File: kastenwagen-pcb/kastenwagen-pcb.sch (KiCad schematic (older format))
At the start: 9 parts

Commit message: Complete Schema
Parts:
- added D100, D101, D120, D121, D140, D141, D160, D170, D181, D202, D203, D222, D223, D242, D243, D262, D272, D273, D304, D305, D324, D325, D344, D345, D364, D374, D375, D406, D407, D437, D446, D457, D476, D477: BAV70, Keebio-Parts:SOT-23_Handsoldering, symbol Diode:BAV70
- added MX101, MX110, MX111, MX120, MX121, MX130, MX131, MX140, MX141, MX150, MX151, MX170, MX171, MX180, MX181, MX203, MX212, MX213, MX222, MX223, MX232, MX233, MX242, MX243, MX252, MX253, MX272, MX273, MX282, MX283, MX305, MX314, MX315, MX324, MX325, MX334, MX335, MX344, MX345, MX354, MX364, MX374, MX375, MX384, MX385, MX416, MX446, MX457, MX467, MX476, MX477, MX486, MX487: MX-NoLED, MX_Only:MXOnly-1U-NoLED, symbol MX_Alps_Hybrid:MX-NoLED
- added MX160, MX304: MX-NoLED, MX_Only:MXOnly-1.75U-NoLED, symbol MX_Alps_Hybrid:MX-NoLED
- added MX202, MX355, MX406, MX407, MX447, MX456: MX-NoLED, MX_Only:MXOnly-1.25U-NoLED, symbol MX_Alps_Hybrid:MX-NoLED
- added MX262: MX-NoLED, MX_Only:MXOnly-1.5U-NoLED, symbol MX_Alps_Hybrid:MX-NoLED
- added MX283.200, MX487.200: MX-NoLED, MX_Only:MXOnly-2U-ReversedStabilizers-NoLED, symbol MX_Alps_Hybrid:MX-NoLED
- added MX417: MX-NoLED, MX_Only:MXOnly-2.75U-NoLED, symbol MX_Alps_Hybrid:MX-NoLED
- added MX417.700: MX-NoLED, MX_Only:MXOnly-7U-NoLED, symbol MX_Alps_Hybrid:MX-NoLED
- added MX437: MX-NoLED, MX_Only:MXOnly-2.25U-NoLED, symbol MX_Alps_Hybrid:MX-NoLED
- added MX477.200: MX-NoLED, MX_Only:MXOnly-2U-NoLED, symbol MX_Alps_Hybrid:MX-NoLED
- added RSW100, RSW181: Rotary_Encoder_Switch, Keebio-Parts:RotaryEncoder_Alps_EC11E-Switch_Vertical_H20mm, symbol Device:Rotary_Encoder_Switch
- D1, D2, D3: footprint (none) -> LED_THT:LED_D3.0mm
- MX100: footprint (none) -> MX_Only:MXOnly-1U-NoLED
- R1, R2, R3: footprint (none) -> Keebio-Parts:Resistor-Hybrid-Back
- SW1: renamed from SW?; footprint (none) -> Keebio-Parts:SW_Tactile_SPST_Angled_MJTP1117
- U1: renamed from U?; footprint (none) -> Keebio-Parts:Elite-C-castellated-29pin-holes
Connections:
- net Col0: now also MX100.1 (COL), U1.20 (A3/PF4), MX101.1 (COL), MX202.1 (COL), MX203.1 (COL), MX304.1 (COL), MX305.1 (COL), MX406.1 (COL), MX407.1 (COL), RSW100.S2
- net Col1: now also U1.19 (A2/PF5), MX110.1 (COL), MX111.1 (COL), MX212.1 (COL), MX213.1 (COL), MX314.1 (COL), MX315.1 (COL), MX416.1 (COL), MX417.1 (COL), MX417.700.1 (COL)
- net Col2: now also U1.18 (A1/PF6), MX120.1 (COL), MX121.1 (COL), MX222.1 (COL), MX223.1 (COL), MX324.1 (COL), MX325.1 (COL)
- net Col3: now also U1.17 (A0/PF7), MX130.1 (COL), MX131.1 (COL), MX232.1 (COL), MX233.1 (COL), MX334.1 (COL), MX335.1 (COL), MX437.1 (COL)
- net Col4: now also U1.16 (15/PB1), MX140.1 (COL), MX141.1 (COL), MX242.1 (COL), MX243.1 (COL), MX344.1 (COL), MX345.1 (COL), MX446.1 (COL), MX447.1 (COL)
- net Col5: now also U1.15 (14/PB3), MX150.1 (COL), MX151.1 (COL), MX252.1 (COL), MX253.1 (COL), MX354.1 (COL), MX355.1 (COL), MX456.1 (COL), MX457.1 (COL)
- net Col6: now also U1.14 (16/PB2), MX160.1 (COL), MX262.1 (COL), MX364.1 (COL), MX467.1 (COL)
- net Col7: now also U1.10 (7/PE6), MX170.1 (COL), MX171.1 (COL), MX272.1 (COL), MX273.1 (COL), MX374.1 (COL), MX375.1 (COL), MX476.1 (COL), MX477.1 (COL), MX477.200.1 (COL)
- net Col8: now also U1.9 (6/PD7), MX180.1 (COL), MX181.1 (COL), MX282.1 (COL), MX283.1 (COL), MX283.200.1 (COL), MX384.1 (COL), MX385.1 (COL), MX486.1 (COL), MX487.1 (COL), MX487.200.1 (COL), RSW181.S2
- net GND: now also RSW100.C, RSW181.C
- net LED1: now also U1.24 (B0)
- net LED2: now also U1.7 (4/PD4)
- net LED3: now also U1.8 (5/PC6)
- net Row0: now also U1.11 (8/PB4), D100.3 (K), D120.3 (K), D140.3 (K), D160.3 (K), D170.3 (K)
- net Row1: now also U1.12 (9/PB5), D101.3 (K), D121.3 (K), D141.3 (K), D181.3 (K)
- net Rotary1A: now reaches U1.1 (TX0/PD3)
- net Rotary1A: now also RSW181.A
- net Row7: now reaches U1.13 (10/PB6)
- net Row7: now also D407.3 (K), D437.3 (K), D457.3 (K), D477.3 (K)
- net Rotary1B: now reaches U1.2 (RX1/PD2)
- net Rotary1B: now also RSW181.B
- net Row2: now reaches U1.25 (B7)
- net Row2: now also D202.3 (K), D222.3 (K), D242.3 (K), D262.3 (K), D272.3 (K)
- net Row3: now reaches U1.26 (D5)
- net Row3: now also D203.3 (K), D223.3 (K), D243.3 (K), D273.3 (K)
- net Row4: now reaches U1.27 (C7)
- net Row4: now also D304.3 (K), D324.3 (K), D344.3 (K), D364.3 (K), D374.3 (K)
- net Row5: now reaches U1.28 (F1)
- net Row5: now also D305.3 (K), D325.3 (K), D345.3 (K), D375.3 (K)
- net Row6: now reaches U1.29 (F0)
- net Row6: now also D406.3 (K), D446.3 (K), D476.3 (K)
- net Rotary0A: now reaches U1.5 (2/PD1)
- net Rotary0A: now also RSW100.A
- net Rotary0B: now reaches U1.6 (3/PD0)
- net Rotary0B: now also RSW100.B
- net at MX100.2 (ROW): now also D100.1 (A), RSW100.S1
- new net: D101.1 (A), MX101.2 (ROW)
- new net: D100.2 (A), MX110.2 (ROW)
- new net: D101.2 (A), MX111.2 (ROW)
- new net: D120.1 (A), MX120.2 (ROW)
- new net: D121.1 (A), MX121.2 (ROW)
- new net: D120.2 (A), MX130.2 (ROW)
- new net: D121.2 (A), MX131.2 (ROW)
- new net: D140.1 (A), MX140.2 (ROW)
- new net: D141.1 (A), MX141.2 (ROW)
- new net: D140.2 (A), MX150.2 (ROW)
- new net: D141.2 (A), MX151.2 (ROW)
- new net: D160.1 (A), MX160.2 (ROW)
- new net: D170.1 (A), MX170.2 (ROW)
- new net: D181.1 (A), MX171.2 (ROW)
- new net: D170.2 (A), MX180.2 (ROW)
- new net: D181.2 (A), MX181.2 (ROW), RSW181.S1
- new net: D202.1 (A), MX202.2 (ROW)
- new net: D203.1 (A), MX203.2 (ROW)
- new net: D202.2 (A), MX212.2 (ROW)
- new net: D203.2 (A), MX213.2 (ROW)
- new net: D222.1 (A), MX222.2 (ROW)
- new net: D223.1 (A), MX223.2 (ROW)
- new net: D222.2 (A), MX232.2 (ROW)
- new net: D223.2 (A), MX233.2 (ROW)
- new net: D242.1 (A), MX242.2 (ROW)
- new net: D243.1 (A), MX243.2 (ROW)
- new net: D242.2 (A), MX252.2 (ROW)
- new net: D243.2 (A), MX253.2 (ROW)
- new net: D262.1 (A), MX262.2 (ROW)
- new net: D272.1 (A), MX272.2 (ROW)
- new net: D273.1 (A), MX273.2 (ROW)
- new net: D272.2 (A), MX282.2 (ROW)
- new net: D273.2 (A), MX283.2 (ROW), MX283.200.2 (ROW)
- new net: D304.1 (A), MX304.2 (ROW)
- new net: D305.1 (A), MX305.2 (ROW)
- new net: D304.2 (A), MX314.2 (ROW)
- new net: D305.2 (A), MX315.2 (ROW)
- new net: D324.1 (A), MX324.2 (ROW)
- new net: D325.1 (A), MX325.2 (ROW)
- new net: D324.2 (A), MX334.2 (ROW)
- new net: D325.2 (A), MX335.2 (ROW)
- new net: D344.1 (A), MX344.2 (ROW)
- new net: D345.1 (A), MX345.2 (ROW)
- new net: D344.2 (A), MX354.2 (ROW)
- new net: D345.2 (A), MX355.2 (ROW)
- new net: D364.1 (A), MX364.2 (ROW)
- new net: D374.1 (A), MX374.2 (ROW)
- new net: D375.1 (A), MX375.2 (ROW)
- new net: D374.2 (A), MX384.2 (ROW)
- new net: D375.2 (A), MX385.2 (ROW)
- new net: D406.1 (A), MX406.2 (ROW)
- new net: D407.1 (A), MX407.2 (ROW)
- new net: D406.2 (A), MX416.2 (ROW)
- new net: D407.2 (A), MX417.2 (ROW), MX417.700.2 (ROW)
- new net: D437.1 (A), MX437.2 (ROW)
- new net: D437.2 (A), MX447.2 (ROW)
- new net: D446.1 (A), MX446.2 (ROW)
- new net: D446.2 (A), MX456.2 (ROW)
- new net: D457.1 (A), MX457.2 (ROW)
- new net: D457.2 (A), MX467.2 (ROW)
- new net: D476.1 (A), MX476.2 (ROW)
- new net: D477.1 (A), MX477.2 (ROW), MX477.200.2 (ROW)
- new net: D476.2 (A), MX486.2 (ROW)
- new net: D477.2 (A), MX487.2 (ROW), MX487.200.2 (ROW)
- no-connect marks 1 -> 4
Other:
- moved on the sheet: D1, D2, D3, MX100, SW1, U1

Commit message: first draft routing
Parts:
- removed MX283.200: MX-NoLED, MX_Only:MXOnly-2U-ReversedStabilizers-NoLED, symbol MX_Alps_Hybrid:MX-NoLED
- RSW100, RSW181: footprint Keebio-Parts:RotaryEncoder_Alps_EC11E-Switch_Vertical_H20mm -> Keebio-Parts:RotaryEncoder_EC11-no-legs
- renumbered D181 to D171
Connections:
- net Rotary0A: now also U1.6 (3/PD0); no longer U1.5 (2/PD1)
- net Rotary0B: now also U1.5 (2/PD1); no longer U1.6 (3/PD0)
- net at MX160.2 (ROW): now also D160.2 (A); no longer D160.1 (A)
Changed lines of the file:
@@
 	1    0    0    -1
 $EndComp
-Wire Wire Line
-	8300 1500 8300 1800
-NoConn ~ 8900 1800
+NoConn ~ 8300 1800
 $Comp
 L MX_Alps_Hybrid:MX-NoLED MX170
@@
 $EndComp
 $Comp
-L Diode:BAV70 D181
+L Diode:BAV70 D171
 U 1 1 6043B80A
 P 10800 1900
-F 0 "D181" H 10800 2117 50  0000 C CNN
+F 0 "D171" H 10800 2117 50  0000 C CNN
 F 1 "BAV70" H 10800 2026 50  0000 C CNN
 F 2 "Keebio-Parts:SOT-23_Handsoldering" H 10800 1900 50  0001 C CNN
@@
 	11150 1300 11150 2500
 Connection ~ 11150 1300
-$Comp
-L MX_Alps_Hybrid:MX-NoLED MX283.200
-U 1 1 6049446A
-P 11950 2850
-F 0 "MX283.200" H 11983 3073 60  0000 C CNN
-F 1 "MX-NoLED" H 11983 2999 20  0000 C CNN
-F 2 "MX_Only:MXOnly-2U-ReversedStabilizers-NoLED" H 11325 2825 60  0001 C CNN
-F 3 "" H 11325 2825 60  0001 C CNN
-	1    11950 2850
-	1    0    0    -1
-$EndComp
-Wire Wire Line
-	12100 2800 12300 2800
-Wire Wire Line
-	12300 2800 12300 2500
-Wire Wire Line
-	12300 2500 11600 2500
-Connection ~ 11600 2500
-Wire Wire Line
-	11900 3000 11900 3400
-Wire Wire Line
-	11900 3400 11400 3400
-Connection ~ 11400 3400
 Text GLabel 1750 3500 0    50   Input ~ 0
 Row2
@@
 F 0 "RSW181" H 12350 1183 50  0000 C CNN
 F 1 "Rotary_Encoder_Switch" H 12350 1274 50  0000 C CNN
-F 2 "Keebio-Parts:RotaryEncoder_Alps_EC11E-Switch_Vertical_H20mm" H 12200 1710 50  0001 C CNN
+F 2 "Keebio-Parts:RotaryEncoder_EC11-no-legs" H 12200 1710 50  0001 C CNN
 F 3 "~" H 12350 1810 50  0001 C CNN
 	1    12350 1550
@@
 Text GLabel 1750 8800 0    50   Input ~ 0
 Rotary1B
+Text GLabel 1750 9200 0    50   Input ~ 0
+Rotary0A
 Text GLabel 1750 9100 0    50   Input ~ 0
-Rotary0A
-Text GLabel 1750 9200 0    50   Input ~ 0
 Rotary0B
 Text GLabel 12650 1650 2    50   Input ~ 0
@@
 F 0 "RSW100" H 1000 1133 50  0000 C CNN
 F 1 "Rotary_Encoder_Switch" H 1000 1224 50  0000 C CNN
-F 2 "Keebio-Parts:RotaryEncoder_Alps_EC11E-Switch_Vertical_H20mm" H 850 1660 50  0001 C CNN
+F 2 "Keebio-Parts:RotaryEncoder_EC11-no-legs" H 850 1660 50  0001 C CNN
 F 3 "~" H 1000 1760 50  0001 C CNN
 	1    1000 1500
@@
 Wire Wire Line
 	5200 10750 5350 10750
+Wire Wire Line
+	8300 1500 8900 1500
+Wire Wire Line
+	8900 1500 8900 1800
 $EndSCHEMATC

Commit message: Reverse the stabilizers
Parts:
- MX417: footprint MX_Only:MXOnly-2.75U-NoLED -> MX_Only:MXOnly-2.75U-ReversedStabilizers-NoLED
- MX417.700: footprint MX_Only:MXOnly-7U-NoLED -> MX_Only:MXOnly-7U-ReversedStabilizers-NoLED
- MX437: footprint MX_Only:MXOnly-2.25U-NoLED -> MX_Only:MXOnly-2.25U-ReversedStabilizers-NoLED
- MX477.200: footprint MX_Only:MXOnly-2U-NoLED -> MX_Only:MXOnly-2U-ReversedStabilizers-NoLED
- MX487.200: footprint MX_Only:MXOnly-2U-ReversedStabilizers-NoLED -> MX_Only:MXOnly-2U-NoLED
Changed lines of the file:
@@
 F 0 "MX417" H 3650 6100 60  0000 C CNN
 F 1 "MX-NoLED" H 3683 5999 20  0000 C CNN
-F 2 "MX_Only:MXOnly-2.75U-NoLED" H 3025 5825 60  0001 C CNN
+F 2 "MX_Only:MXOnly-2.75U-ReversedStabilizers-NoLED" H 3025 5825 60  0001 C CNN
 F 3 "" H 3025 5825 60  0001 C CNN
 	1    3650 5850
@@
 F 0 "MX487.200" H 11983 6073 60  0000 C CNN
 F 1 "MX-NoLED" H 11983 5999 20  0000 C CNN
-F 2 "MX_Only:MXOnly-2U-ReversedStabilizers-NoLED" H 11325 5825 60  0001 C CNN
+F 2 "MX_Only:MXOnly-2U-NoLED" H 11325 5825 60  0001 C CNN
 F 3 "" H 11325 5825 60  0001 C CNN
 	1    11950 5850
@@
 F 0 "MX417.700" H 4100 6100 60  0000 C CNN
 F 1 "MX-NoLED" H 4133 5999 20  0000 C CNN
-F 2 "MX_Only:MXOnly-7U-NoLED" H 3475 5825 60  0001 C CNN
+F 2 "MX_Only:MXOnly-7U-ReversedStabilizers-NoLED" H 3475 5825 60  0001 C CNN
 F 3 "" H 3475 5825 60  0001 C CNN
 	1    4100 5850
@@
 F 0 "MX437" H 5250 6100 60  0000 C CNN
 F 1 "MX-NoLED" H 5283 5999 20  0000 C CNN
-F 2 "MX_Only:MXOnly-2.25U-NoLED" H 4625 5825 60  0001 C CNN
+F 2 "MX_Only:MXOnly-2.25U-ReversedStabilizers-NoLED" H 4625 5825 60  0001 C CNN
 F 3 "" H 4625 5825 60  0001 C CNN
 	1    5250 5850
@@
 F 0 "MX477.200" H 10000 6100 60  0000 C CNN
 F 1 "MX-NoLED" H 10033 5999 20  0000 C CNN
-F 2 "MX_Only:MXOnly-2U-NoLED" H 9375 5825 60  0001 C CNN
+F 2 "MX_Only:MXOnly-2U-ReversedStabilizers-NoLED" H 9375 5825 60  0001 C CNN
 F 3 "" H 9375 5825 60  0001 C CNN
 	1    10000 5850

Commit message: drawing edge cuts
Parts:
- D1, D2, D3: footprint LED_THT:LED_D3.0mm -> LED_SMD:LED_1206_3216Metric_Pad1.42x1.75mm_HandSolder
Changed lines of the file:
@@
 F 0 "D1" H 5043 9795 50  0000 C CNN
 F 1 "LED" H 5043 9886 50  0000 C CNN
-F 2 "LED_THT:LED_D3.0mm" H 5050 10050 50  0001 C CNN
+F 2 "LED_SMD:LED_1206_3216Metric_Pad1.42x1.75mm_HandSolder" H 5050 10050 50  0001 C CNN
 F 3 "~" H 5050 10050 50  0001 C CNN
 	1    5050 10050
@@
 F 0 "D2" H 5043 10145 50  0000 C CNN
 F 1 "LED" H 5043 10236 50  0000 C CNN
-F 2 "LED_THT:LED_D3.0mm" H 5050 10400 50  0001 C CNN
+F 2 "LED_SMD:LED_1206_3216Metric_Pad1.42x1.75mm_HandSolder" H 5050 10400 50  0001 C CNN
 F 3 "~" H 5050 10400 50  0001 C CNN
 	1    5050 10400
@@
 F 0 "D3" H 5043 10495 50  0000 C CNN
 F 1 "LED" H 5043 10586 50  0000 C CNN
-F 2 "LED_THT:LED_D3.0mm" H 5050 10750 50  0001 C CNN
+F 2 "LED_SMD:LED_1206_3216Metric_Pad1.42x1.75mm_HandSolder" H 5050 10750 50  0001 C CNN
 F 3 "~" H 5050 10750 50  0001 C CNN
 	1    5050 10750

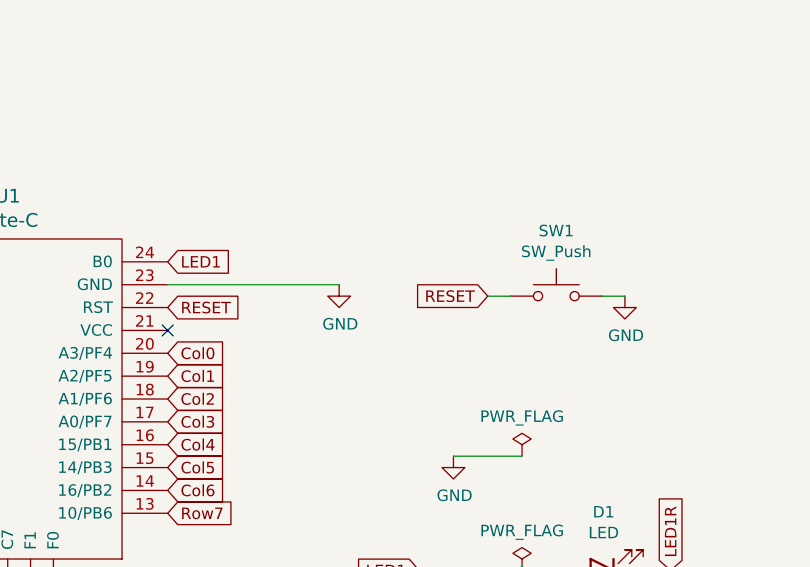
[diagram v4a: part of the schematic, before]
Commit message: Ground planes
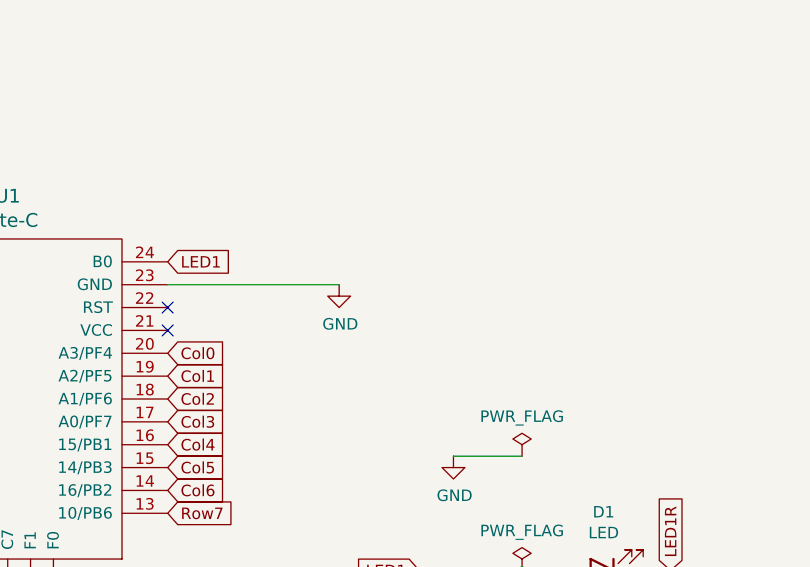
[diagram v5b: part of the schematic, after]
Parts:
- removed SW1: SW_Push, Keebio-Parts:SW_Tactile_SPST_Angled_MJTP1117, symbol Switch:SW_Push
- R1, R2, R3: footprint Keebio-Parts:Resistor-Hybrid-Back -> Keebio-Parts:R_0805
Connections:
- net RESET: no longer names the net of U1.22 (RST)
- no-connect marks 4 -> 5
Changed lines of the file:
@@
 Wire Wire Line
 	3900 8800 3150 8800
-$Comp
-L Switch:SW_Push SW1
-U 1 1 60414731
-P 4850 8850
-F 0 "SW1" H 4850 9135 50  0000 C CNN
-F 1 "SW_Push" H 4850 9044 50  0000 C CNN
-F 2 "Keebio-Parts:SW_Tactile_SPST_Angled_MJTP1117" H 4850 9050 50  0001 C CNN
-F 3 "~" H 4850 9050 50  0001 C CNN
-	1    4850 8850
-	1    0    0    -1
-$EndComp
-Text GLabel 3150 8900 2    50   Input ~ 0
-RESET
-Text GLabel 4550 8850 0    50   Input ~ 0
-RESET
-Wire Wire Line
-	4550 8850 4650 8850
-$Comp
-L power:GND #PWR0104
-U 1 1 60414DCC
-P 5150 8850
-F 0 "#PWR0104" H 5150 8600 50  0001 C CNN
-F 1 "GND" H 5155 8677 50  0000 C CNN
-F 2 "" H 5150 8850 50  0001 C CNN
-F 3 "" H 5150 8850 50  0001 C CNN
-	1    5150 8850
-	1    0    0    -1
-$EndComp
-Wire Wire Line
-	5150 8850 5050 8850
 NoConn ~ 3150 9000
 $Comp
@@
 F 0 "R1" V 6493 10050 50  0000 C CNN
 F 1 "470" V 6584 10050 50  0000 C CNN
-F 2 "Keebio-Parts:Resistor-Hybrid-Back" V 6630 10050 50  0001 C CNN
+F 2 "Keebio-Parts:R_0805" V 6630 10050 50  0001 C CNN
 F 3 "~" H 6700 10050 50  0001 C CNN
 	1    6700 10050
@@
 F 0 "R2" V 6493 10400 50  0000 C CNN
 F 1 "470" V 6584 10400 50  0000 C CNN
-F 2 "Keebio-Parts:Resistor-Hybrid-Back" V 6630 10400 50  0001 C CNN
+F 2 "Keebio-Parts:R_0805" V 6630 10400 50  0001 C CNN
 F 3 "~" H 6700 10400 50  0001 C CNN
 	1    6700 10400
@@
 F 0 "R3" V 6493 10750 50  0000 C CNN
 F 1 "470" V 6584 10750 50  0000 C CNN
-F 2 "Keebio-Parts:Resistor-Hybrid-Back" V 6630 10750 50  0001 C CNN
+F 2 "Keebio-Parts:R_0805" V 6630 10750 50  0001 C CNN
 F 3 "~" H 6700 10750 50  0001 C CNN
 	1    6700 10750
@@
 Wire Wire Line
 	8900 1500 8900 1800
+NoConn ~ 3150 8900
 $EndSCHEMATC

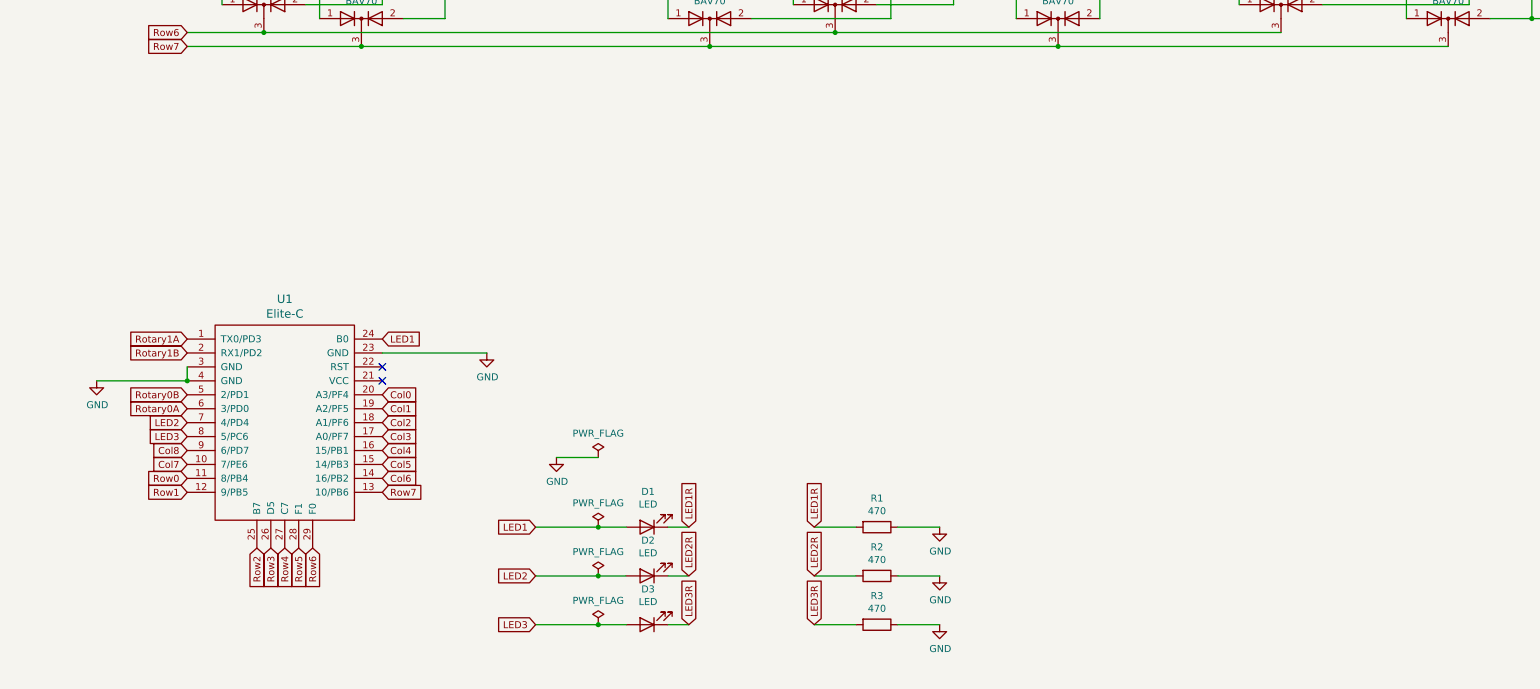
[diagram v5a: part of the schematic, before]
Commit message: On-board MCU to universal daughterboard
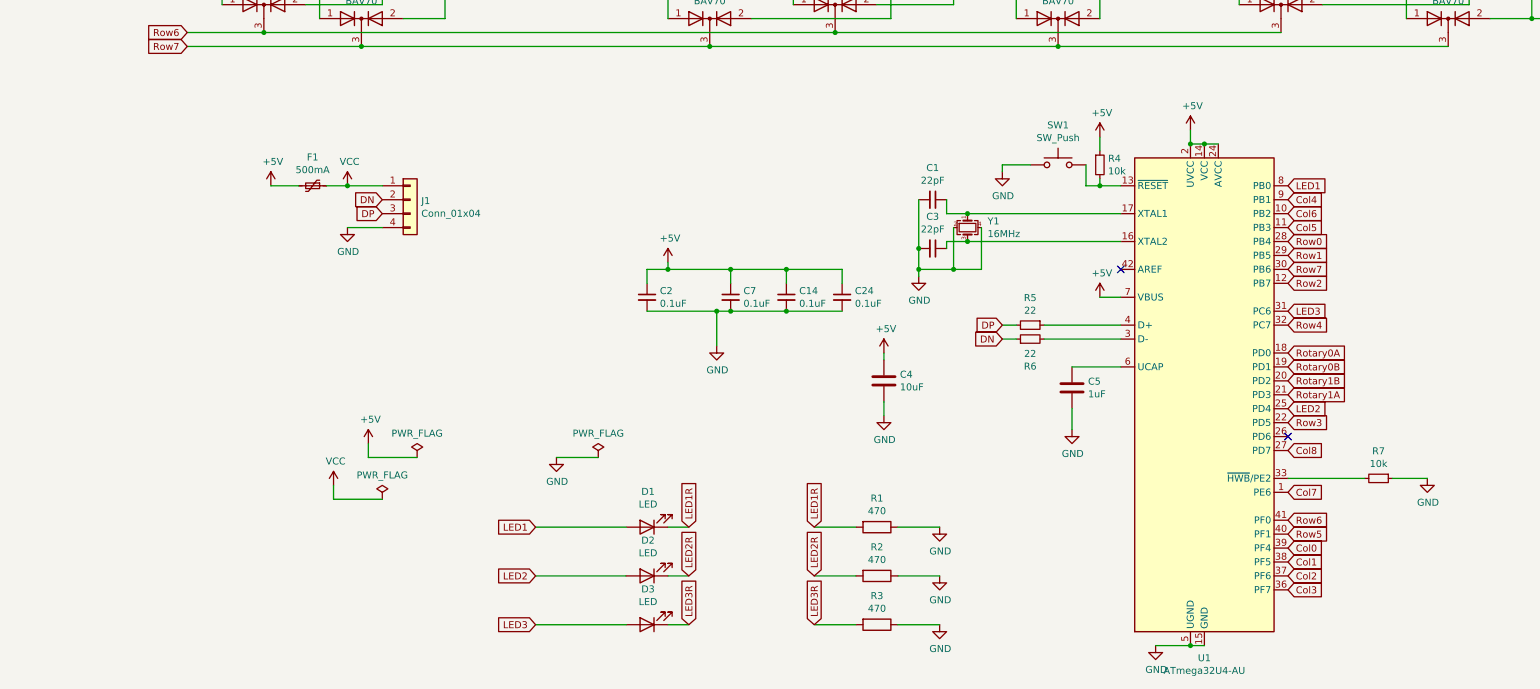
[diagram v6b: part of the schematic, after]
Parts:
- removed U1: Elite-C, Keebio-Parts:Elite-C-castellated-29pin-holes, symbol keebio:Elite-C
- added C1, C3: 22pF, Capacitor_SMD:C_0805_2012Metric, symbol Device:C_Small
- added C14, C2, C24, C7: 0.1uF, Capacitor_SMD:C_0805_2012Metric, symbol Device:C_Small
- added C4: 10uF, Capacitor_SMD:C_0805_2012Metric, symbol Device:C
- added C5: 1uF, Capacitor_SMD:C_0805_2012Metric, symbol Device:C
- added F1: 500mA, Fuse:Fuse_1206_3216Metric, symbol Device:Polyfuse_Small
- added J1: Conn_01x04, random-keyboard-parts:JST-SR-4, symbol Connector_Generic:Conn_01x04
- added R4, R7: 10k, Keebio-Parts:R_0805, symbol Device:R_Small
- added R5, R6: 22, Keebio-Parts:R_0805, symbol Device:R_Small
- added SW1: SW_Push, Button_Switch_SMD:SW_Push_1P1T_NO_6x6mm_H9.5mm, symbol Switch:SW_Push
- added U1: ATmega32U4-AU, Package_QFP:TQFP-44_10x10mm_P0.8mm, symbol MCU_Microchip_ATmega:ATmega32U4-AU
- added Y1: 16MHz, Crystal:Crystal_SMD_3225-4Pin_3.2x2.5mm, symbol Device:Crystal_GND24_Small
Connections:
- net Col0: now also U1.39 (PF4)
- net Col1: now also U1.38 (PF5)
- net Col2: now also U1.37 (PF6)
- net Col3: now also U1.36 (PF7)
- net Col4: now also U1.9 (PB1)
- net Col5: now also U1.11 (PB3)
- net Col6: now also U1.10 (PB2)
- net Col7: now also U1.1 (PE6)
- net Col8: now also U1.27 (PD7)
- net GND: now also C1.2, C14.2, C2.2, C24.2, C3.2, C4.2, C5.2, C7.2, J1.4 (Pin_4), R7.1, SW1.1, U1.15 (GND), U1.23 (GND), U1.35 (GND), U1.43 (GND), U1.5 (UGND), Y1.2, Y1.4
- net LED1: now also U1.8 (PB0)
- net LED2: now also U1.25 (PD4)
- net LED3: now also U1.31 (PC6)
- net Rotary0A: now also U1.18 (PD0)
- net Rotary0B: now also U1.19 (PD1)
- net Rotary1A: now also U1.21 (PD3)
- net Rotary1B: now also U1.20 (PD2)
- net Row0: now also U1.28 (PB4)
- net Row1: now also U1.29 (PB5)
- net Row2: now also U1.12 (PB7)
- net Row3: now also U1.22 (PD5)
- net Row4: now also U1.32 (PC7)
- net Row5: now also U1.40 (PF1)
- net Row6: now also U1.41 (PF0)
- net Row7: now also U1.30 (PB6)
- new net: R4.2, SW1.2, U1.13 (~RESET)
- new net: C3.1, U1.16 (XTAL2), Y1.3
- new net: C1.1, U1.17 (XTAL1), Y1.1
- new net: R6.2, U1.3 (D-)
- new net: R7.2, U1.33 (~HWB~/PE2)
- new net: R5.1, U1.4 (D+)
- new net: C5.1, U1.6 (UCAP)
- new net +5V: C14.1, C2.1, C24.1, C4.1, C7.1, F1.2, R4.1, U1.14 (VCC), U1.2 (UVCC), U1.24 (AVCC), U1.34 (VCC), U1.44 (AVCC), U1.7 (VBUS)
- new net DN: J1.2 (Pin_2), R6.1
- new net DP: J1.3 (Pin_3), R5.2
- new net VCC: F1.1, J1.1 (Pin_1)
